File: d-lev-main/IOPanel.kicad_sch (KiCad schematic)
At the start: 11 parts, among them J1 PJ-059A, J3 USB_C_Receptacle_USB2.0, J4 AudioJack3, J5 DIN-41524, U2 FT230XS, U4 AMS1117-5.0, U5 AMS1117-3.3, X1 SGAS15A12-P1J

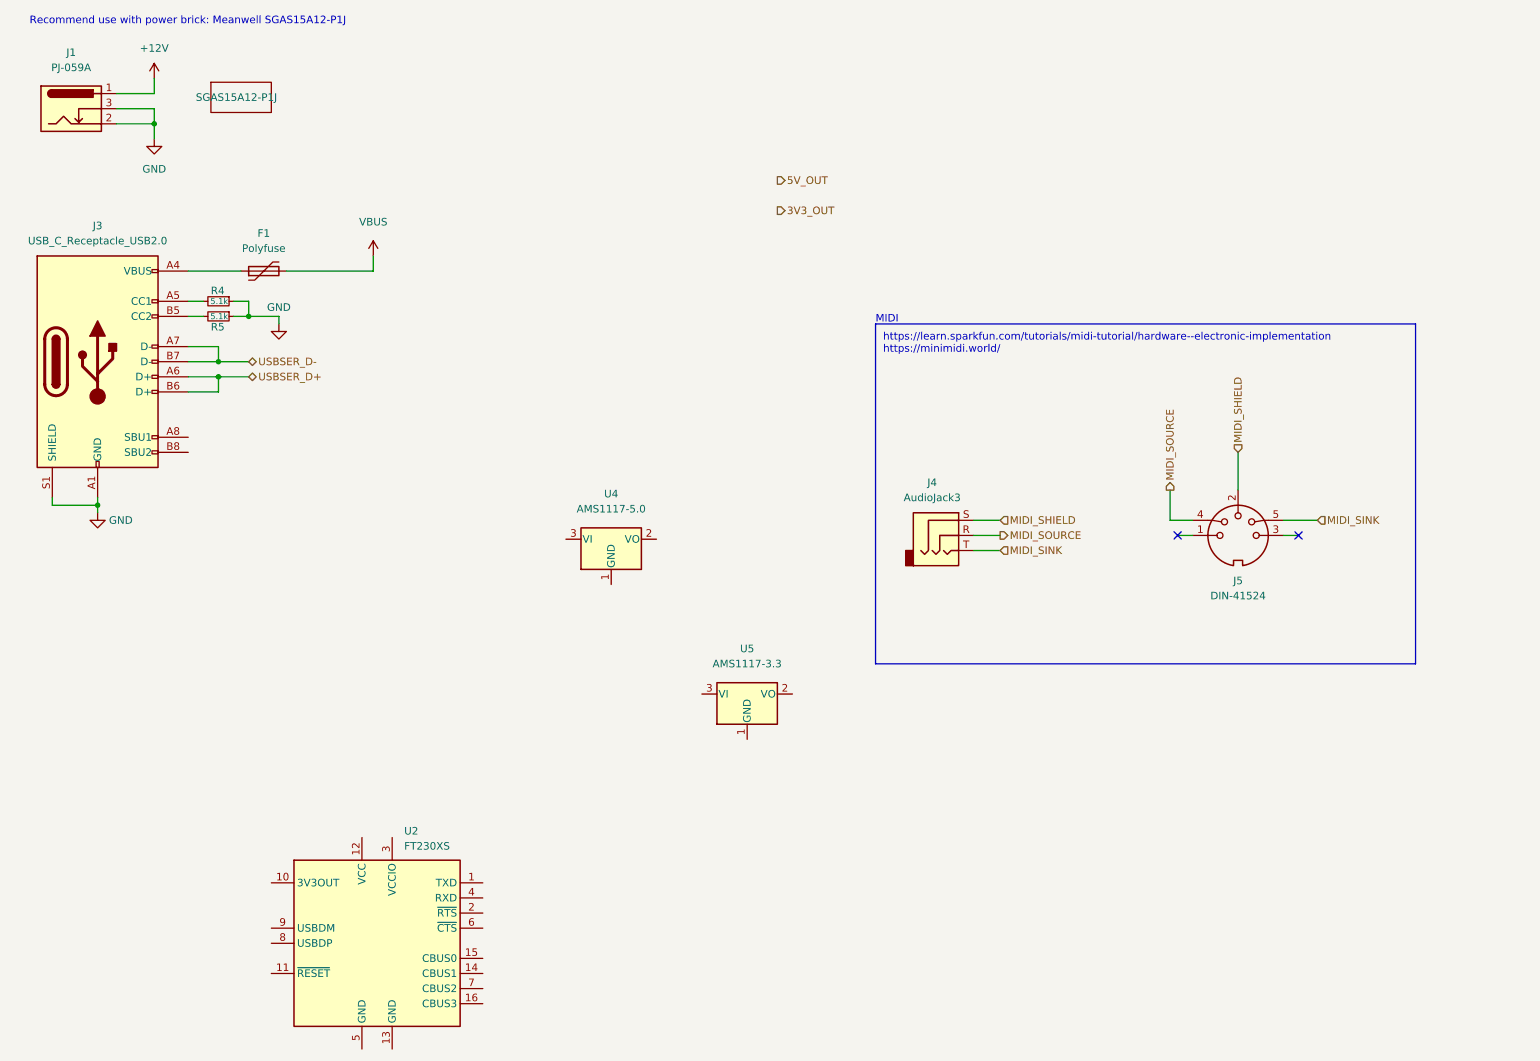
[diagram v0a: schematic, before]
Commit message: Add block diagram
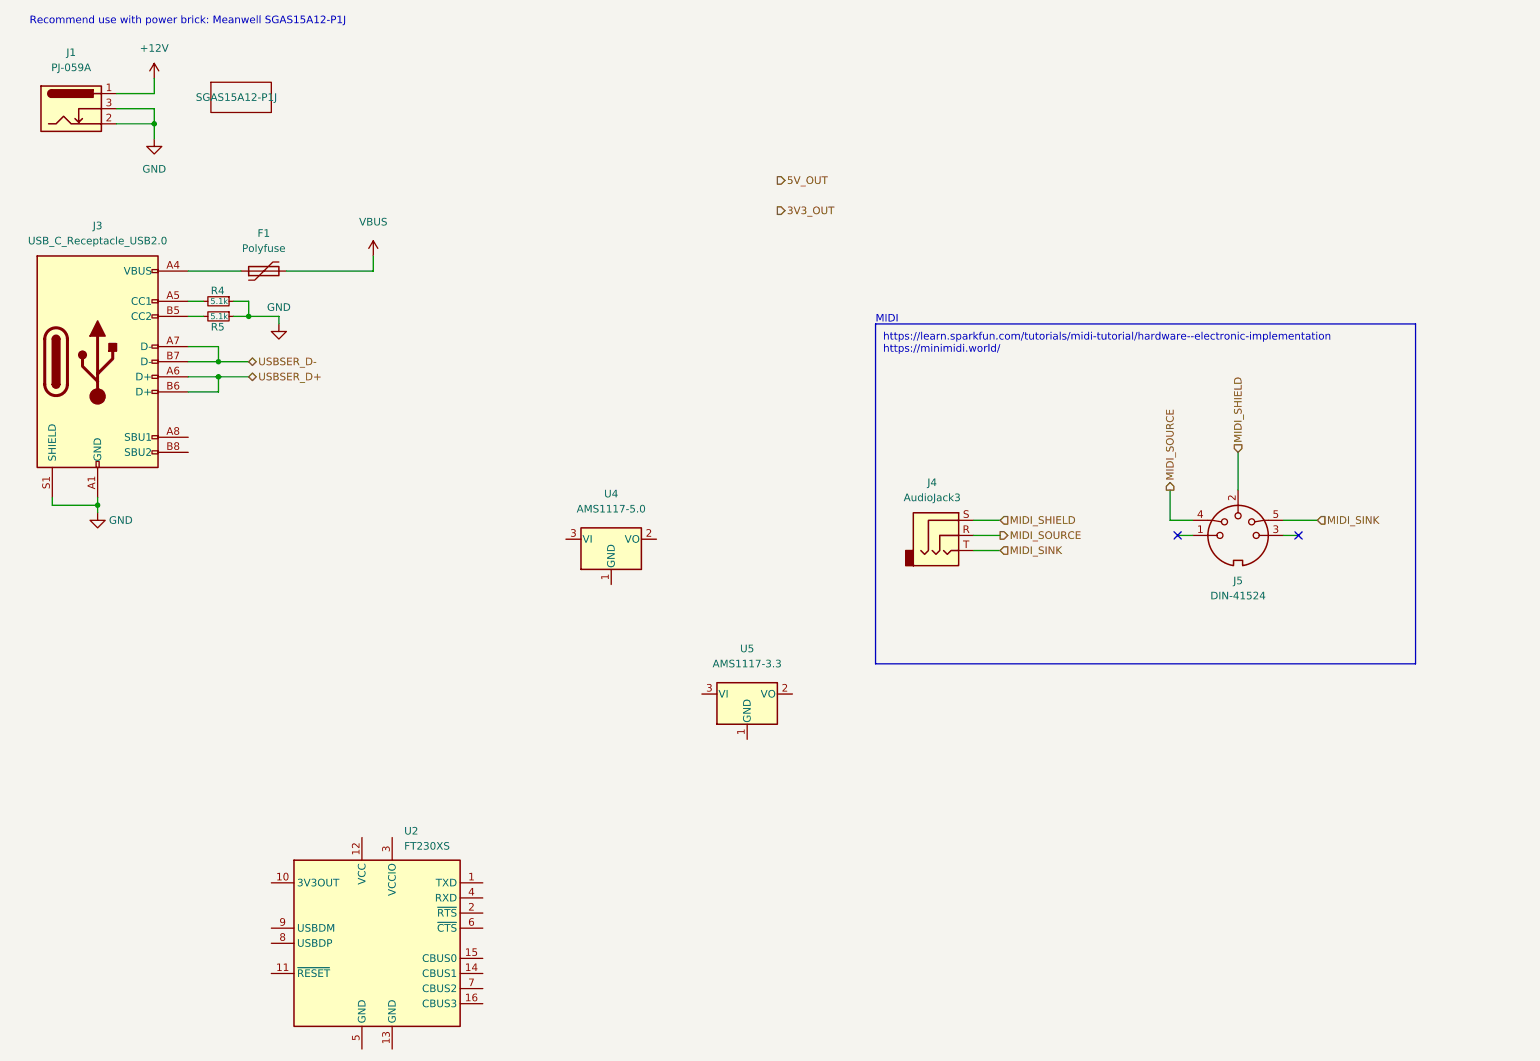
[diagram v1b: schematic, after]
